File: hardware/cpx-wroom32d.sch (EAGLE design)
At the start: 37 parts, among them Q1 mmbt2222, Q2 mmbt2222, U1 ESP32-WROOM-32D, X2 ESP32_WROOM32_SKINNY

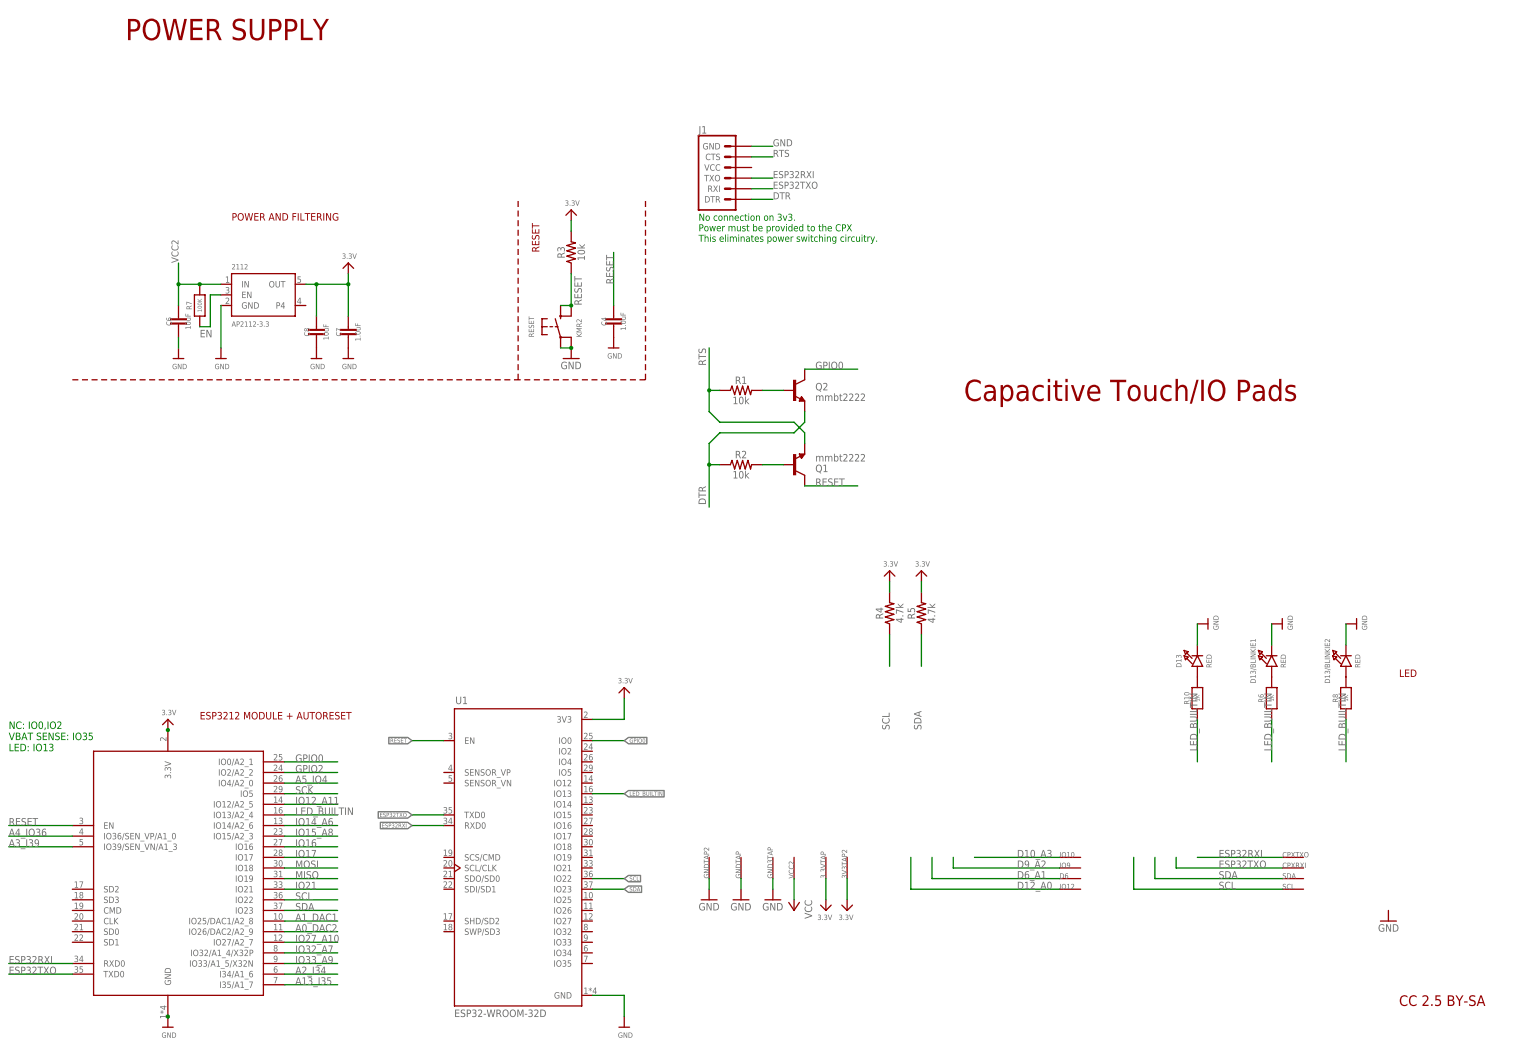
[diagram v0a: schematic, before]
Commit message: About to remove some connections to the CPX.
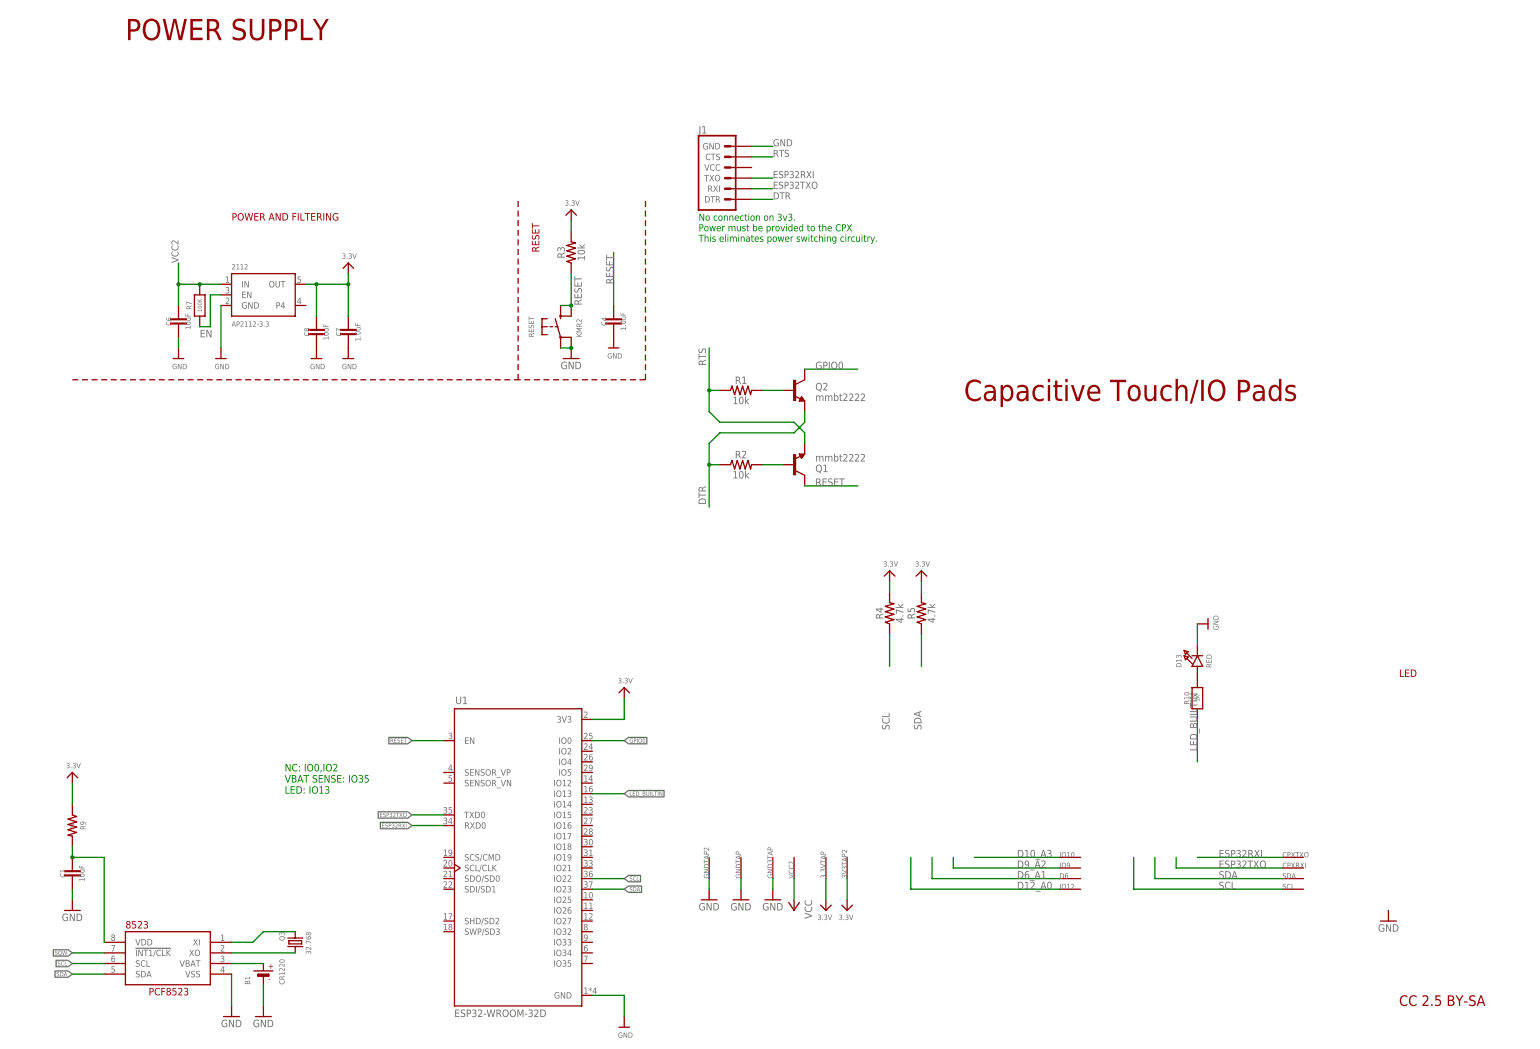
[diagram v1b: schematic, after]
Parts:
- removed D13/BLINKIE1, D13/BLINKIE2: RED, microbuilder:LED0805_NOOUTLINE
- removed R6, R8: 1K, microbuilder:RESISTOR_0603_NOOUT
- removed X2: ESP32_WROOM32_SKINNY, microbuilder:ESP32_WROOM32_SKINNY
- added 8523: RTC_PCF8523T, microbuilder:RTC_PCF8523T
- added B1: CR1220, microbuilder:BATTERYCR1220_SMT
- added C1: 10uF, SparkFun-Capacitors:10UF-0603-6.3V-20%
- added Q3: 32.768, microbuilder:CRYSTAL8.0X3.8
- added R9: 1k, SparkFun-Resistors:1KOHM-0603-1/10W-1%
- J1: device SparkFun-Connectors:6_PIN_SERIAL_TARGET -> SparkFun-Connectors:6_PIN_SERIAL_TARGETRA_SMT
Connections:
- removed net A0_DAC2: X2.IO26/DAC2/A2_9
- removed net A13_I35: X2.I35/A1_7
- removed net A1_DAC1: X2.IO25/DAC1/A2_8
- removed net A2_I34: X2.I34/A1_6
- removed net A3_I39: X2.IO39/SEN_VN/A1_3
- removed net A4_IO36: X2.IO36/SEN_VP/A1_0
- removed net A5_IO4: X2.IO4/A2_0
- removed net GPIO2: X2.IO2/A2_2
- removed net IO12_A11: X2.IO12/A2_5
- removed net IO14_A6: X2.IO14/A2_6
- removed net IO15_A8: X2.IO15/A2_3
- removed net IO16: X2.IO16
- removed net IO17: X2.IO17
- removed net IO21: X2.IO21
- removed net IO27_A10: X2.IO27/A2_7
- removed net IO32_A7: X2.IO32/A1_4/X32P
- removed net IO33_A9: X2.IO33/A1_5/X32N
- removed net MISO: X2.IO19
- removed net MOSI: X2.IO18
- removed net N$1: D13/BLINKIE1.A, R6.2
- removed net N$2: D13/BLINKIE2.A, R8.2
- removed net SCK: X2.IO5
- new net CLKVCC: 8523.VDD, C1.1, R9.2
- new net SQW: 8523.!INT1/CLK
- new net VBAT1: 8523.VBAT, B1.+
- new net XI: 8523.XI, Q3.1
- new net XO: 8523.XO, Q3.2
- net 3.3V: now also R9.1; no longer X2.3.3V
- net ESP32RXI: no longer X2.RXD0
- net ESP32TXO: no longer X2.TXD0
- net GND: now also 8523.VSS, B1.-, C1.2; no longer D13/BLINKIE1.C, D13/BLINKIE2.C, X2.GND
- net GPIO0: no longer X2.IO0/A2_1
- net LED_BUILTIN: no longer R6.1, R8.1, X2.IO13/A2_4
- net RESET: no longer X2.EN
- net SCL: now also 8523.SCL; no longer X2.IO22
- net SDA: now also 8523.SDA; no longer X2.IO23
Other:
- note removed: "ESP3212 MODULE + AUTORESET"

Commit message: Routed.
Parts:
- renumbered B1 to CR1220, Q3 to XTAL
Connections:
- net 3.3V: no longer 3.3VTAP.SEW, 3V3TAP2.SEW
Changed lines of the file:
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@@
 <part name="GND21" library="supply1" deviceset="GND" device=""/>
 <part name="GND13" library="supply1" deviceset="GND" device=""/>
-<part name="U$29" library="microbuilder" deviceset="3.3V" device=""/>
 <part name="U$40" library="microbuilder" deviceset="FRAME_A3_ADAFRUIT" device=""/>
-<part name="U$41" library="microbuilder" deviceset="3.3V" device=""/>
 <part name="GND8" library="supply1" deviceset="GND" device=""/>
 <part name="C6" library="SparkFun-Capacitors" library_urn="urn:adsk.eagle:library:510" deviceset="10UF" device="-0603-6.3V-20%" package3d_urn="urn:adsk.eagle:package:37414/1" value="10uF"/>
@@
 <part name="U$6" library="microbuilder" deviceset="3.3V" device=""/>
 <part name="U$7" library="microbuilder" deviceset="GND" device=""/>
-<part name="Q3" library="microbuilder" deviceset="CRYSTAL" device="8.0X3.8" value="32.768"/>
+<part name="XTAL" library="microbuilder" deviceset="CRYSTAL" device="8.0X3.8" value="32.768"/>
 <part name="GND16" library="supply1" deviceset="GND" device=""/>
 <part name="GND17" library="supply1" deviceset="GND" device=""/>
 <part name="C1" library="SparkFun-Capacitors" library_urn="urn:adsk.eagle:library:510" deviceset="10UF" device="-0603-6.3V-20%" package3d_urn="urn:adsk.eagle:package:37414/1" value="10uF"/>
 <part name="GND2" library="supply1" deviceset="GND" device=""/>
-<part name="B1" library="microbuilder" deviceset="BATTERY" device="CR1220_SMT" value="CR1220"/>
+<part name="CR1220" library="microbuilder" deviceset="BATTERY" device="CR1220_SMT" value="CR1220"/>
 <part name="8523" library="microbuilder" deviceset="RTC_PCF8523" device="T"/>
 <part name="R9" library="SparkFun-Resistors" library_urn="urn:adsk.eagle:library:532" deviceset="1KOHM" device="-0603-1/10W-1%" package3d_urn="urn:adsk.eagle:package:39650/1" value="1k"/>
@@
 <attribute name="VALUE" x="193.04" y="38.1" size="1.778" layer="96"/>
 </instance>
-<instance part="U$29" gate="G$1" x="208.28" y="38.1" smashed="yes" rot="R180">
-<attribute name="VALUE" x="209.804" y="37.084" size="1.27" layer="96" rot="R180"/>
-</instance>
 <instance part="U$40" gate="G$1" x="0" y="0" smashed="yes">
 <attribute name="DRAWING_NAME" x="298.45" y="15.24" size="2.54" layer="94" font="vector"/>
@@
 <attribute name="SHEET" x="357.505" y="10.16" size="2.54" layer="94" font="vector"/>
 </instance>
-<instance part="U$41" gate="G$1" x="213.36" y="38.1" smashed="yes" rot="R180">
-<attribute name="VALUE" x="214.884" y="37.084" size="1.27" layer="96" rot="R180"/>
-</instance>
 <instance part="GND8" gate="1" x="342.9" y="35.56" smashed="yes" rot="MR0">
 <attribute name="VALUE" x="345.44" y="33.02" size="1.778" layer="96" rot="MR0"/>
@@
 <attribute name="VALUE" x="158.496" y="7.62" size="1.27" layer="96"/>
 </instance>
-<instance part="Q3" gate="G$1" x="81.28" y="30.48" smashed="yes" rot="MR270">
+<instance part="XTAL" gate="G$1" x="81.28" y="30.48" smashed="yes" rot="MR270">
 <attribute name="NAME" x="78.74" y="33.02" size="1.27" layer="95" rot="MR270"/>
 <attribute name="VALUE" x="85.09" y="33.02" size="1.27" layer="96" rot="MR270"/>
@@
 <attribute name="VALUE" x="25.4" y="35.56" size="1.778" layer="96"/>
 </instance>
-<instance part="B1" gate="G$1" x="73.66" y="22.86" smashed="yes" rot="R90">
+<instance part="CR1220" gate="G$1" x="73.66" y="22.86" smashed="yes" rot="R90">
 <attribute name="NAME" x="70.485" y="20.32" size="1.27" layer="95" rot="R90"/>
 <attribute name="VALUE" x="78.74" y="20.32" size="1.27" layer="96" rot="R90"/>
@@
 <wire x1="73.66" y1="20.32" x2="73.66" y2="15.24" width="0.1524" layer="91"/>
 <pinref part="GND17" gate="1" pin="GND"/>
-<pinref part="B1" gate="G$1" pin="-"/>
+<pinref part="CR1220" gate="G$1" pin="-"/>
 </segment>
 <segment>
@@
 </net>
 <net name="3.3V" class="0">
-<segment>
-<pinref part="3.3VTAP" gate="G$1" pin="SEW"/>
-<wire x1="208.28" y1="40.64" x2="208.28" y2="45.72" width="0.1524" layer="91"/>
-<pinref part="U$29" gate="G$1" pin="3.3V"/>
-</segment>
-<segment>
-<pinref part="U$41" gate="G$1" pin="3.3V"/>
-<pinref part="3V3TAP2" gate="G$1" pin="SEW"/>
-<wire x1="213.36" y1="40.64" x2="213.36" y2="45.72" width="0.1524" layer="91"/>
-</segment>
 <segment>
 <wire x1="83.82" y1="187.96" x2="86.36" y2="187.96" width="0.1524" layer="91"/>
@@
 <net name="XI" class="0">
 <segment>
-<pinref part="Q3" gate="G$1" pin="1"/>
+<pinref part="XTAL" gate="G$1" pin="1"/>
 <pinref part="8523" gate="G$1" pin="XI"/>
 <wire x1="81.28" y1="33.02" x2="73.66" y2="33.02" width="0.1524" layer="91"/>
@@
 <segment>
 <wire x1="81.28" y1="27.94" x2="66.04" y2="27.94" width="0.1524" layer="91"/>
-<pinref part="Q3" gate="G$1" pin="2"/>
+<pinref part="XTAL" gate="G$1" pin="2"/>
 <pinref part="8523" gate="G$1" pin="XO"/>
 </segment>
@@
 <segment>
 <wire x1="73.66" y1="25.4" x2="66.04" y2="25.4" width="0.1524" layer="91"/>
-<pinref part="B1" gate="G$1" pin="+"/>
+<pinref part="CR1220" gate="G$1" pin="+"/>
 <pinref part="8523" gate="G$1" pin="VBAT"/>
 </segment>

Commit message: Looks goo.
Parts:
- added BME680: BME280, microbuilder:BME280
- added FRAME1: FRAME-LETTERNO_PACKAGE, SparkFun-Aesthetics:FRAME-LETTERNO_PACKAGE
- R4, R5: value 4.7k -> 10K
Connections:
- new net SDO/ADR: BME680.SDO
- net 3.3V: now also BME680.CSB, BME680.VDD, BME680.VDDIO
- net GND: now also BME680.GND
- net SCL: now also BME680.SCK
- net SDA: now also BME680.SDI
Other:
- note added: "BME680 AIR QUALITY SENSOR"
- note added: "ESP32 WROOM 32D"
- note added: "FTDI"
- note added: "NOTE: The 3V3 pads are NOT connected. The reason: This eliminates complexity in the power circuit, and prevents accidents where power is applied incorrectly or in multiple places."
- note added: "NOTE: The VCC line is NOT CONNECTED. This means that the shield MUST be connected to either a CPX that is being powered, OR it must be powered at ~5V via VCC."
- note added: "PADS, PULLUPS, AND LED"
- note added: "PCF8523 RTC"
- note added: "RESET CIRCUITRY"
- note added: "This RTC runs at 3.3V, which is the single most important thing to know about it. It is not the same as the DS1307 or DS3231, but it is similar (w.r.t. I2C commands), lower voltage, and cheaper."
- note added: "This part can do I2C or SPI. For I2C, CSB should be pulled HIGH. Then: * SDI == SDA * SCK == SDL"
- note removed: "CC 2.5 BY-SA"
- note removed: "Capacitive Touch/IO Pads"
- note removed: "LED"
- note removed: "NC: IO0,IO2 VBAT SENSE: IO35 LED: IO13"
- note removed: "POWER SUPPLY"
- moved on the sheet: 2112, 3.3VTAP, 3V3TAP2, 8523, C1, C4, C6, C7, C8, CPXRXI, CPXTXO, CR1220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
